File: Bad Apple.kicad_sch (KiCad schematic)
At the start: 0 parts

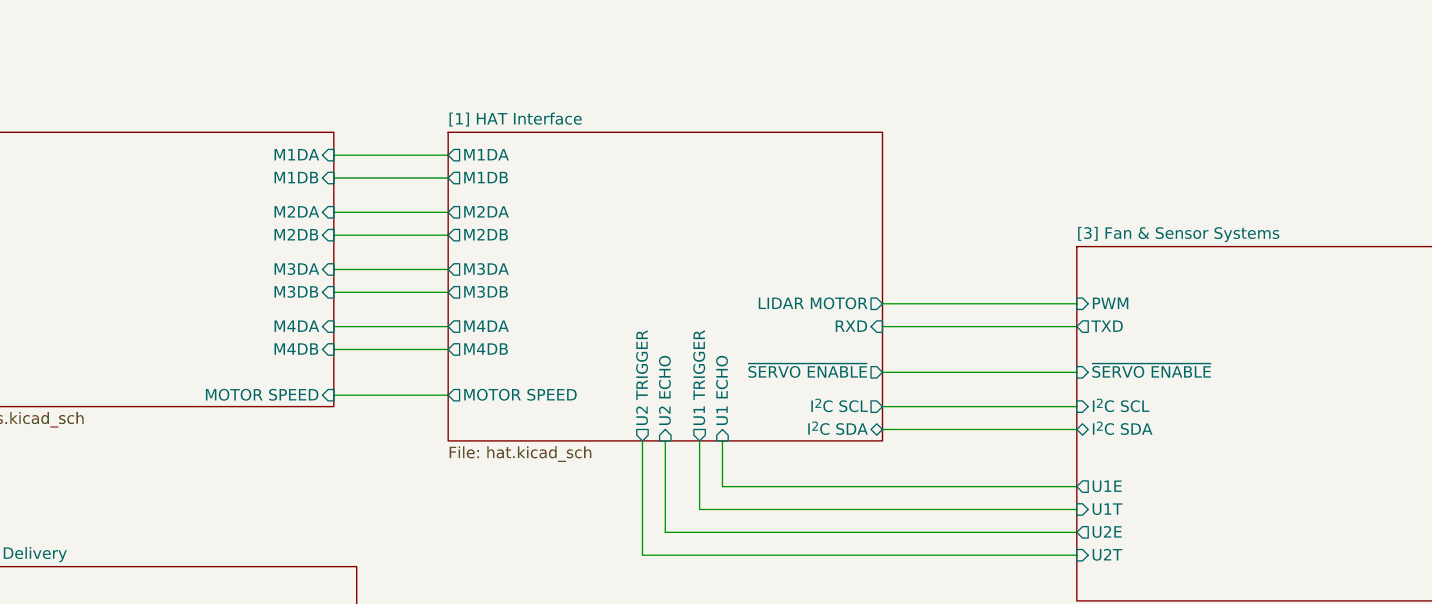
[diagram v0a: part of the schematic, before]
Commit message: feat(pcb): made the fan controlled by a NPN transistor
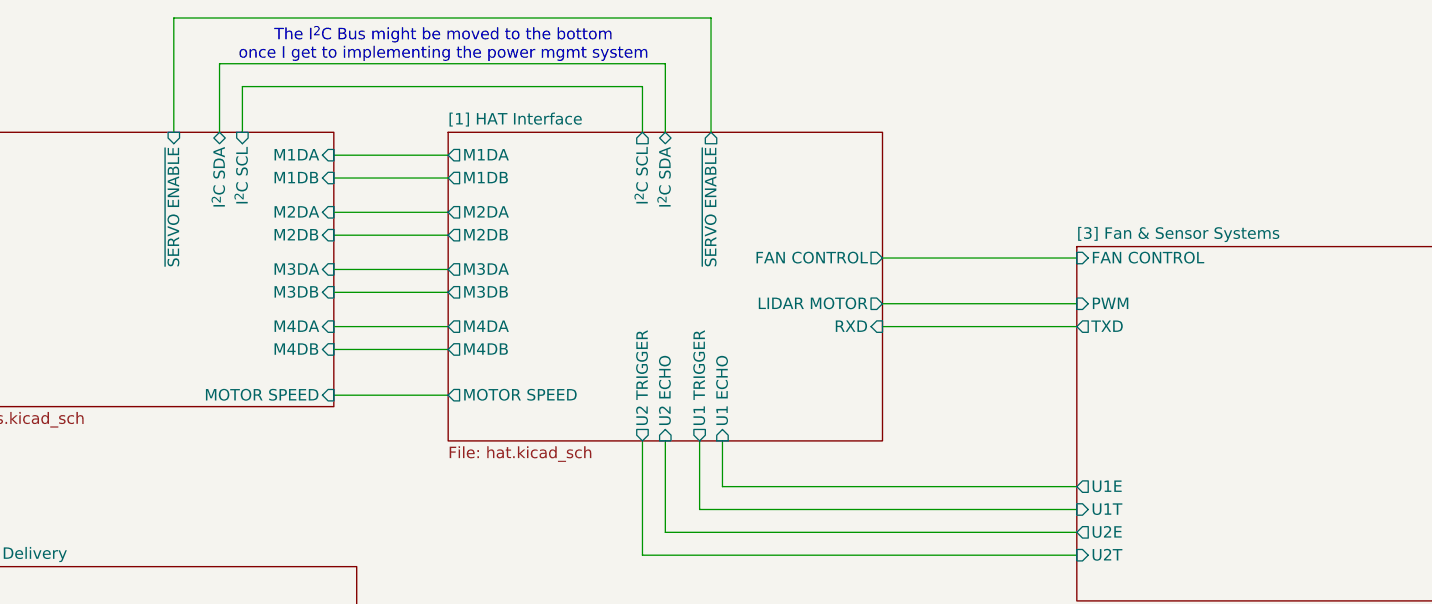
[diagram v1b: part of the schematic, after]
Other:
- sheet [1] HAT Interface ports: added FAN CONTROL; removed none
- sheet [3] Fan & Sensor Systems ports: added FAN CONTROL; removed I^{2}C SCL, I^{2}C SDA, ~{SERVO ENABLE}
- sheet [4] Motors ports: added I^{2}C SCL, I^{2}C SDA, ~{SERVO ENABLE}; removed none
- note added: "The I^{2}C Bus might be moved to the bottom once I get to implementing the power mgmt system"
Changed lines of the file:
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@@
 		(comment 4 "Schematic Overview")
 	)
+	(text "The I^{2}C Bus might be moved to the bottom\nonce I get to implementing the power mgmt system"
+		(exclude_from_sim no)
+		(at 112.522 62.738 0)
+		(effects
+			(font
+				(size 1.27 1.27)
+			)
+		)
+	)
+	(wire
+		(pts
+			(xy 137.16 64.77) (xy 137.16 72.39)
+		)
+		(stroke
+			(width 0)
+			(type default)
+		)
+	)
+	(wire
+		(pts
+			(xy 142.24 59.69) (xy 82.55 59.69)
+		)
+		(stroke
+			(width 0)
+			(type default)
+		)
+	)
+	(wire
+		(pts
+			(xy 134.62 72.39) (xy 134.62 67.31)
+		)
+		(stroke
+			(width 0)
+			(type default)
+		)
+	)
+	(wire
+		(pts
+			(xy 87.63 72.39) (xy 87.63 64.77)
+		)
+		(stroke
+			(width 0)
+			(type default)
+		)
+	)
 	(wire
 		(pts
@@
 	(wire
 		(pts
+			(xy 90.17 67.31) (xy 90.17 72.39)
+		)
+		(stroke
+			(width 0)
+			(type default)
+		)
+	)
+	(wire
+		(pts
 			(xy 161.29 93.98) (xy 182.88 93.98)
 		)
@@
 	(wire
 		(pts
-			(xy 161.29 105.41) (xy 182.88 105.41)
-		)
-		(stroke
-			(width 0)
-			(type default)
-		)
-	)
-	(wire
-		(pts
-			(xy 161.29 102.87) (xy 182.88 102.87)
+			(xy 134.62 67.31) (xy 90.17 67.31)
+		)
+		(stroke
+			(width 0)
+			(type default)
+		)
+	)
+	(wire
+		(pts
+			(xy 87.63 64.77) (xy 137.16 64.77)
 		)
 		(stroke
@@
 	(wire
 		(pts
+			(xy 82.55 59.69) (xy 82.55 72.39)
+		)
+		(stroke
+			(width 0)
+			(type default)
+		)
+	)
+	(wire
+		(pts
 			(xy 143.51 111.76) (xy 182.88 111.76)
 		)
@@
 	(wire
 		(pts
+			(xy 142.24 72.39) (xy 142.24 59.69)
+		)
+		(stroke
+			(width 0)
+			(type default)
+		)
+	)
+	(wire
+		(pts
 			(xy 100.33 74.93) (xy 113.03 74.93)
 		)
@@
 	(wire
 		(pts
-			(xy 161.29 99.06) (xy 182.88 99.06)
-		)
-		(stroke
-			(width 0)
-			(type default)
-		)
-	)
-	(wire
-		(pts
 			(xy 100.33 93.98) (xy 113.03 93.98)
 		)
@@
 		(pts
 			(xy 100.33 96.52) (xy 113.03 96.52)
+		)
+		(stroke
+			(width 0)
+			(type default)
+		)
+	)
+	(wire
+		(pts
+			(xy 161.29 86.36) (xy 182.88 86.36)
 		)
 		(stroke
@@
 			)
 		)
-		(pin "I^{2}C SCL" output
-			(at 161.29 102.87 0)
-			(effects
-				(font
-					(size 1.27 1.27)
-				)
-				(justify right)
-			)
-		)
-		(pin "I^{2}C SDA" bidirectional
-			(at 161.29 105.41 0)
-			(effects
-				(font
-					(size 1.27 1.27)
-				)
-				(justify right)
-			)
-		)
 		(pin "M1DA" output
 			(at 113.03 74.93 180)
@@
 			)
 		)
-		(pin "~{SERVO ENABLE}" output
-			(at 161.29 99.06 0)
-			(effects
-				(font
-					(size 1.27 1.27)
-				)
-				(justify right)
-			)
-		)
 		(pin "MOTOR SPEED" output
 			(at 113.03 101.6 180)
@@
 				)
 				(justify left)
+			)
+		)
+		(pin "FAN CONTROL" output
+			(at 161.29 86.36 0)
+			(effects
+				(font
+					(size 1.27 1.27)
+				)
+				(justify right)
+			)
+		)
+		(pin "I^{2}C SCL" output
+			(at 134.62 72.39 90)
+			(effects
+				(font
+					(size 1.27 1.27)
+				)
+				(justify right)
+			)
+		)
+		(pin "I^{2}C SDA" bidirectional
+			(at 137.16 72.39 90)
+			(effects
+				(font
+					(size 1.27 1.27)
+				)
+				(justify right)
+			)
+		)
+		(pin "~{SERVO ENABLE}" output
+			(at 142.24 72.39 90)
+			(effects
+				(font
+					(size 1.27 1.27)
+				)
+				(justify right)
 			)
 		)
@@
 			)
 		)
-		(pin "~{SERVO ENABLE}" input
-			(at 182.88 99.06 180)
-			(effects
-				(font
-					(size 1.27 1.27)
-				)
-				(justify left)
-			)
-		)
-		(pin "I^{2}C SCL" input
-			(at 182.88 102.87 180)
-			(effects
-				(font
-					(size 1.27 1.27)
-				)
-				(justify left)
-			)
-		)
-		(pin "I^{2}C SDA" bidirectional
-			(at 182.88 105.41 180)
+		(pin "FAN CONTROL" input
+			(at 182.88 86.36 180)
 			(effects
 				(font
@@
 			(effects
 				(font
+					(size 1.27 1.27)
+				)
+				(justify right)
+			)
+		)
+		(pin "I^{2}C SCL" input
+			(at 90.17 72.39 90)
+			(effects
+				(font
+					(size 1.27 1.27)
+				)
+				(justify right)
+			)
+		)
+		(pin "I^{2}C SDA" bidirectional
+			(at 87.63 72.39 90)
+			(effects
+				(font
+					(size 1.27 1.27)
+				)
+				(justify right)
+			)
+		)
+		(pin "~{SERVO ENABLE}" input
+			(at 82.55 72.39 90)
+			(effects
+				(font

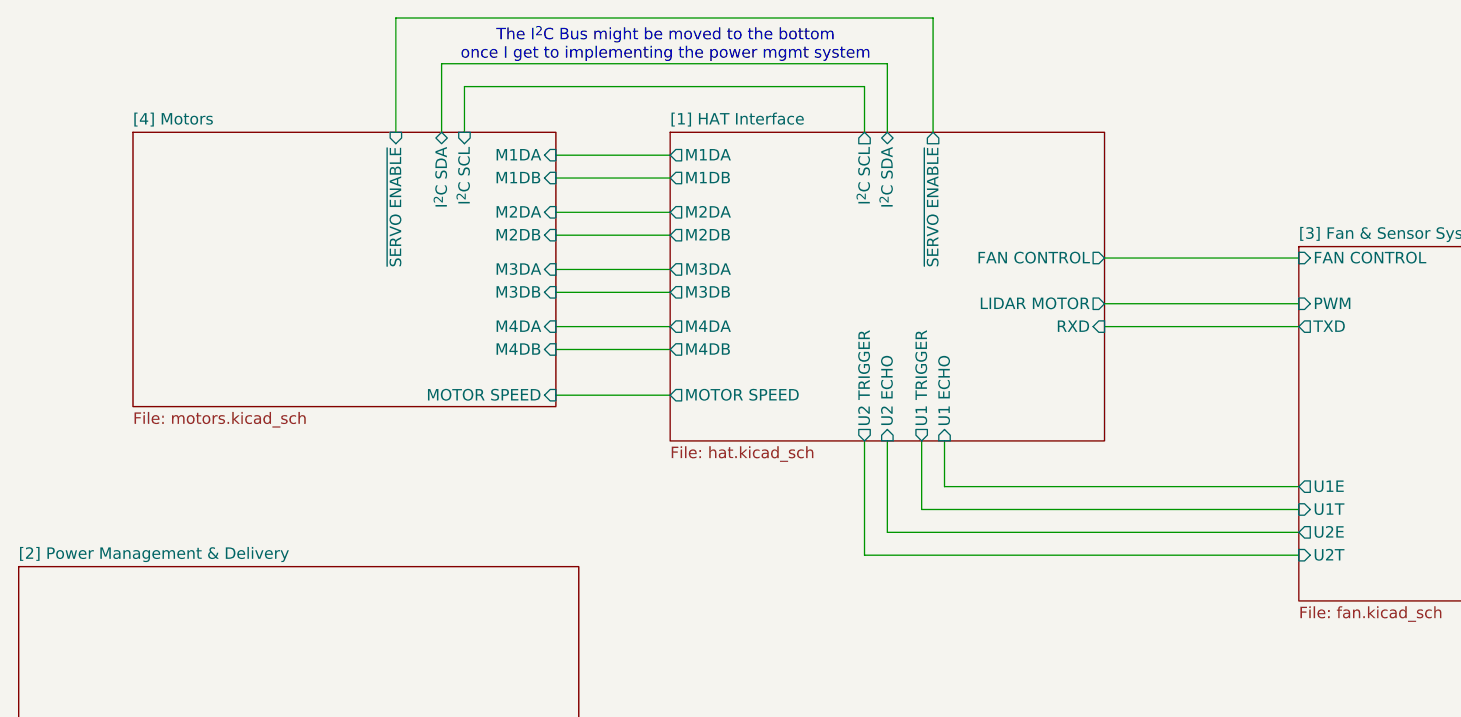
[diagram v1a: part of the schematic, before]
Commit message: doc(pcb): added docs for some of the main components of the HAT
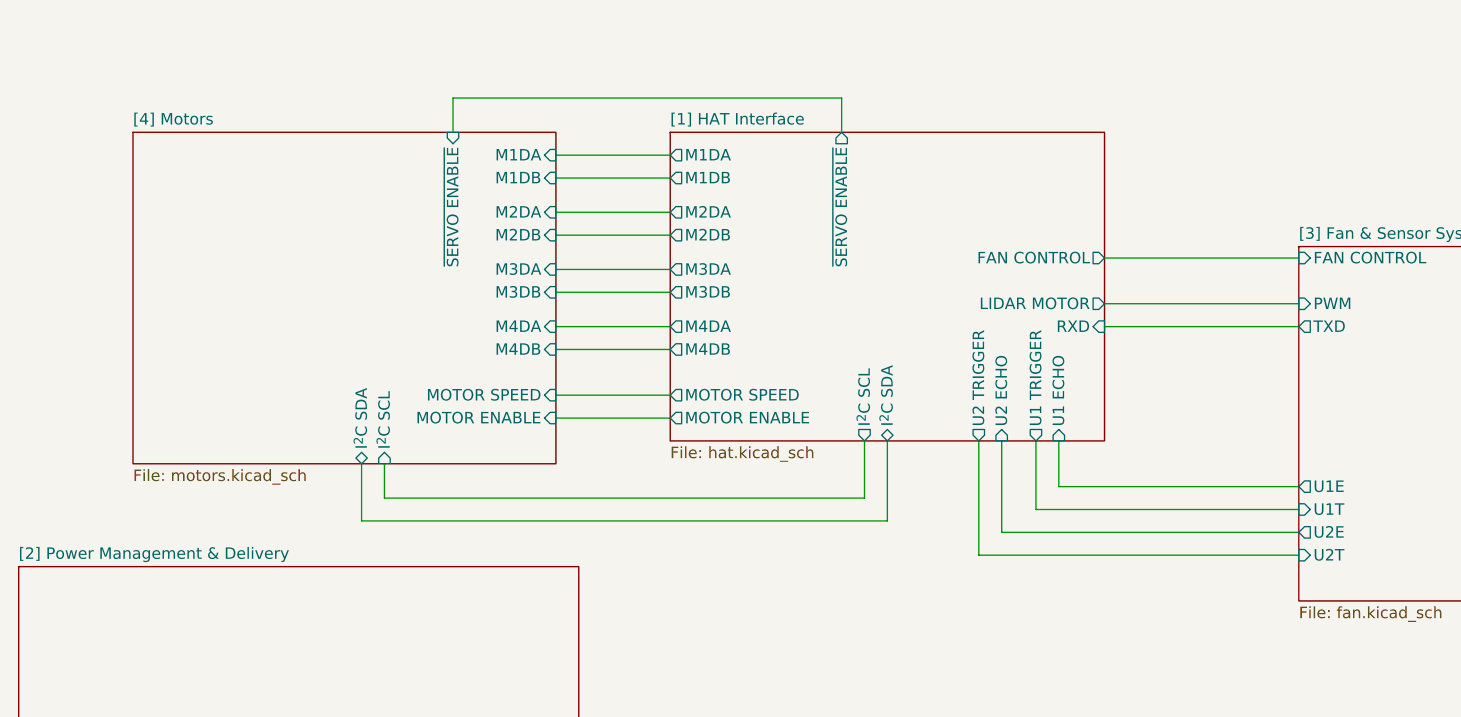
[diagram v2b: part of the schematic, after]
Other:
- sheet [1] HAT Interface ports: added MOTOR ENABLE; removed none
- sheet [4] Motors ports: added MOTOR ENABLE; removed none
- note removed: "The I^{2}C Bus might be moved to the bottom once I get to implementing the power mgmt system"
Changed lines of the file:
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@@
 		(comment 4 "Schematic Overview")
 	)
-	(text "The I^{2}C Bus might be moved to the bottom\nonce I get to implementing the power mgmt system"
-		(exclude_from_sim no)
-		(at 112.522 62.738 0)
-		(effects
-			(font
-				(size 1.27 1.27)
-			)
-		)
-	)
-	(wire
-		(pts
-			(xy 137.16 64.77) (xy 137.16 72.39)
-		)
-		(stroke
-			(width 0)
-			(type default)
-		)
-	)
-	(wire
-		(pts
-			(xy 142.24 59.69) (xy 82.55 59.69)
-		)
-		(stroke
-			(width 0)
-			(type default)
-		)
-	)
-	(wire
-		(pts
-			(xy 134.62 72.39) (xy 134.62 67.31)
-		)
-		(stroke
-			(width 0)
-			(type default)
-		)
-	)
-	(wire
-		(pts
-			(xy 87.63 72.39) (xy 87.63 64.77)
+	(wire
+		(pts
+			(xy 81.28 113.03) (xy 134.62 113.03)
+		)
+		(stroke
+			(width 0)
+			(type default)
+		)
+	)
+	(wire
+		(pts
+			(xy 137.16 115.57) (xy 78.74 115.57)
 		)
 		(stroke
@@
 	(wire
 		(pts
-			(xy 143.51 106.68) (xy 143.51 111.76)
-		)
-		(stroke
-			(width 0)
-			(type default)
-		)
-	)
-	(wire
-		(pts
-			(xy 137.16 116.84) (xy 182.88 116.84)
+			(xy 88.9 68.58) (xy 132.08 68.58)
+		)
+		(stroke
+			(width 0)
+			(type default)
+		)
+	)
+	(wire
+		(pts
+			(xy 156.21 106.68) (xy 156.21 111.76)
+		)
+		(stroke
+			(width 0)
+			(type default)
+		)
+	)
+	(wire
+		(pts
+			(xy 149.86 116.84) (xy 182.88 116.84)
+		)
+		(stroke
+			(width 0)
+			(type default)
+		)
+	)
+	(wire
+		(pts
+			(xy 134.62 106.68) (xy 134.62 113.03)
 		)
 		(stroke
@@
 	(wire
 		(pts
-			(xy 134.62 106.68) (xy 134.62 119.38)
-		)
-		(stroke
-			(width 0)
-			(type default)
-		)
-	)
-	(wire
-		(pts
-			(xy 90.17 67.31) (xy 90.17 72.39)
+			(xy 147.32 106.68) (xy 147.32 119.38)
+		)
+		(stroke
+			(width 0)
+			(type default)
+		)
+	)
+	(wire
+		(pts
+			(xy 78.74 109.22) (xy 78.74 115.57)
 		)
 		(stroke
@@
 	(wire
 		(pts
-			(xy 134.62 67.31) (xy 90.17 67.31)
-		)
-		(stroke
-			(width 0)
-			(type default)
-		)
-	)
-	(wire
-		(pts
-			(xy 87.63 64.77) (xy 137.16 64.77)
-		)
-		(stroke
-			(width 0)
-			(type default)
-		)
-	)
-	(wire
-		(pts
 			(xy 161.29 91.44) (xy 182.88 91.44)
 		)
@@
 	(wire
 		(pts
-			(xy 134.62 119.38) (xy 182.88 119.38)
+			(xy 147.32 119.38) (xy 182.88 119.38)
+		)
+		(stroke
+			(width 0)
+			(type default)
+		)
+	)
+	(wire
+		(pts
+			(xy 100.33 104.14) (xy 113.03 104.14)
 		)
 		(stroke
@@
 	(wire
 		(pts
-			(xy 82.55 59.69) (xy 82.55 72.39)
-		)
-		(stroke
-			(width 0)
-			(type default)
-		)
-	)
-	(wire
-		(pts
-			(xy 143.51 111.76) (xy 182.88 111.76)
+			(xy 156.21 111.76) (xy 182.88 111.76)
 		)
 		(stroke
@@
 	(wire
 		(pts
-			(xy 140.97 114.3) (xy 182.88 114.3)
-		)
-		(stroke
-			(width 0)
-			(type default)
-		)
-	)
-	(wire
-		(pts
-			(xy 142.24 72.39) (xy 142.24 59.69)
+			(xy 153.67 114.3) (xy 182.88 114.3)
 		)
 		(stroke
@@
 	(wire
 		(pts
-			(xy 137.16 106.68) (xy 137.16 116.84)
+			(xy 149.86 106.68) (xy 149.86 116.84)
 		)
 		(stroke
@@
 	(wire
 		(pts
+			(xy 132.08 68.58) (xy 132.08 72.39)
+		)
+		(stroke
+			(width 0)
+			(type default)
+		)
+	)
+	(wire
+		(pts
 			(xy 161.29 86.36) (xy 182.88 86.36)
 		)
@@
 	(wire
 		(pts
-			(xy 140.97 106.68) (xy 140.97 114.3)
+			(xy 137.16 106.68) (xy 137.16 115.57)
+		)
+		(stroke
+			(width 0)
+			(type default)
+		)
+	)
+	(wire
+		(pts
+			(xy 88.9 72.39) (xy 88.9 68.58)
+		)
+		(stroke
+			(width 0)
+			(type default)
+		)
+	)
+	(wire
+		(pts
+			(xy 153.67 106.68) (xy 153.67 114.3)
 		)
 		(stroke
@@
 		(pts
 			(xy 100.33 77.47) (xy 113.03 77.47)
+		)
+		(stroke
+			(width 0)
+			(type default)
+		)
+	)
+	(wire
+		(pts
+			(xy 81.28 109.22) (xy 81.28 113.03)
 		)
 		(stroke
@@
 		)
 		(pin "U1 ECHO" input
-			(at 143.51 106.68 270)
+			(at 156.21 106.68 270)
 			(effects
 				(font
@@
 		)
 		(pin "U1 TRIGGER" output
-			(at 140.97 106.68 270)
+			(at 153.67 106.68 270)
 			(effects
 				(font
@@
 		)
 		(pin "U2 ECHO" input
-			(at 137.16 106.68 270)
+			(at 149.86 106.68 270)
 			(effects
 				(font
@@
 		)
 		(pin "U2 TRIGGER" output
-			(at 134.62 106.68 270)
+			(at 147.32 106.68 270)
 			(effects
 				(font
@@
 		)
 		(pin "I^{2}C SCL" output
-			(at 134.62 72.39 90)
-			(effects
-				(font
-					(size 1.27 1.27)
-				)
-				(justify right)
+			(at 134.62 106.68 270)
+			(effects
+				(font
+					(size 1.27 1.27)
+				)
+				(justify left)
 			)
 		)
 		(pin "I^{2}C SDA" bidirectional
-			(at 137.16 72.39 90)
-			(effects
-				(font
-					(size 1.27 1.27)
-				)
-				(justify right)
+			(at 137.16 106.68 270)
+			(effects
+				(font
+					(size 1.27 1.27)
+				)
+				(justify left)
 			)
 		)
 		(pin "~{SERVO ENABLE}" output
-			(at 142.24 72.39 90)
-			(effects
-				(font
-					(size 1.27 1.27)
-				)
-				(justify right)
+			(at 132.08 72.39 90)
+			(effects
+				(font
+					(size 1.27 1.27)
+				)
+				(justify right)
+			)
+		)
+		(pin "MOTOR ENABLE" output
+			(at 113.03 104.14 180)
+			(effects
+				(font
+					(size 1.27 1.27)
+				)
+				(justify left)
 			)
 		)
@@
 	(sheet
 		(at 53.34 72.39)
-		(size 46.99 30.48)
+		(size 46.99 36.83)
 		(exclude_from_sim no)
 		(in_bom yes)
@@
 		)
 		(property "Sheetfile" "motors.kicad_sch"
-			(at 53.34 103.4546 0)
+			(at 53.34 109.8046 0)
 			(effects
 				(font
@@
 		)
 		(pin "I^{2}C SCL" input
-			(at 90.17 72.39 90)
-			(effects
-				(font
-					(size 1.27 1.27)
-				)
-				(justify right)
+			(at 81.28 109.22 270)
+			(effects
+				(font
+					(size 1.27 1.27)
+				)
+				(justify left)
 			)
 		)
 		(pin "I^{2}C SDA" bidirectional
-			(at 87.63 72.39 90)
-			(effects
-				(font
-					(size 1.27 1.27)
-				)
-				(justify right)
+			(at 78.74 109.22 270)
+			(effects
+				(font
+					(size 1.27 1.27)
+				)
+				(justify left)
 			)
 		)
 		(pin "~{SERVO ENABLE}" input
-			(at 82.55 72.39 90)
-			(effects
-				(font
+			(at 88.9 72.39 90)
+			(effects
+				(font
+					(size 1.27 1.27)
+				)
+				(justify right)
+			)
+		)
+		(pin "MOTOR ENABLE" input
+			(at 100.33 104.14 0)
+			(effects
+				(font

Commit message: chore(pcb)??: i forgor what this commit does lmao
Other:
- note added: "1) Raspberry Pi/Main System"
- note added: "2) Power Supply A (5V 4A)"
- note added: "3) Power Supply B (12V 8A)"
- note added: "4) IMU"
- note added: "5) Motor Driver"
- note added: "Datasheet Overview"
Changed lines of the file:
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@@
 		(comment 4 "Schematic Overview")
+	)
+	(text "3) Power Supply B (12V 8A)"
+		(exclude_from_sim no)
+		(at 240.03 24.13 0)
+		(effects
+			(font
+				(size 1.27 1.27)
+			)
+			(justify left)
+		)
+	)
+	(text "Datasheet Overview"
+		(exclude_from_sim no)
+		(at 261.62 15.494 0)
+		(effects
+			(font
+				(size 1.524 1.524)
+				(thickness 0.3048)
+				(bold yes)
+			)
+			(justify right)
+		)
+	)
+	(text "5) Motor Driver"
+		(exclude_from_sim no)
+		(at 240.03 29.21 0)
+		(effects
+			(font
+				(size 1.27 1.27)
+				(thickness 0.1588)
+			)
+			(justify left)
+			(href "https://cdn.sparkfun.com/assets/0/1/b/b/3/TB6612FNG.pdf")
+		)
+	)
+	(text "2) Power Supply A (5V 4A)"
+		(exclude_from_sim no)
+		(at 240.03 21.59 0)
+		(effects
+			(font
+				(size 1.27 1.27)
+				(thickness 0.1588)
+			)
+			(justify left)
+		)
+	)
+	(text "4) IMU"
+		(exclude_from_sim no)
+		(at 240.03 26.67 0)
+		(effects
+			(font
+				(size 1.27 1.27)
+				(thickness 0.1588)
+			)
+			(justify left)
+			(href "https://jlcpcb.com/api/file/downloadByFileSystemAccessId/8588905297688088576")
+		)
+	)
+	(text "1) Raspberry Pi/Main System"
+		(exclude_from_sim no)
+		(at 240.03 19.05 0)
+		(effects
+			(font
+				(size 1.27 1.27)
+				(thickness 0.1588)
+			)
+			(justify left)
+			(href "https://datasheets.raspberrypi.com/rpi4/raspberry-pi-4-datasheet.pdf")
+		)
 	)
 	(wire
